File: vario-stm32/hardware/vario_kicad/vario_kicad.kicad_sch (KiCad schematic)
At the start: 2 parts, among them U1 STM32L071CBTx, U2 BME280

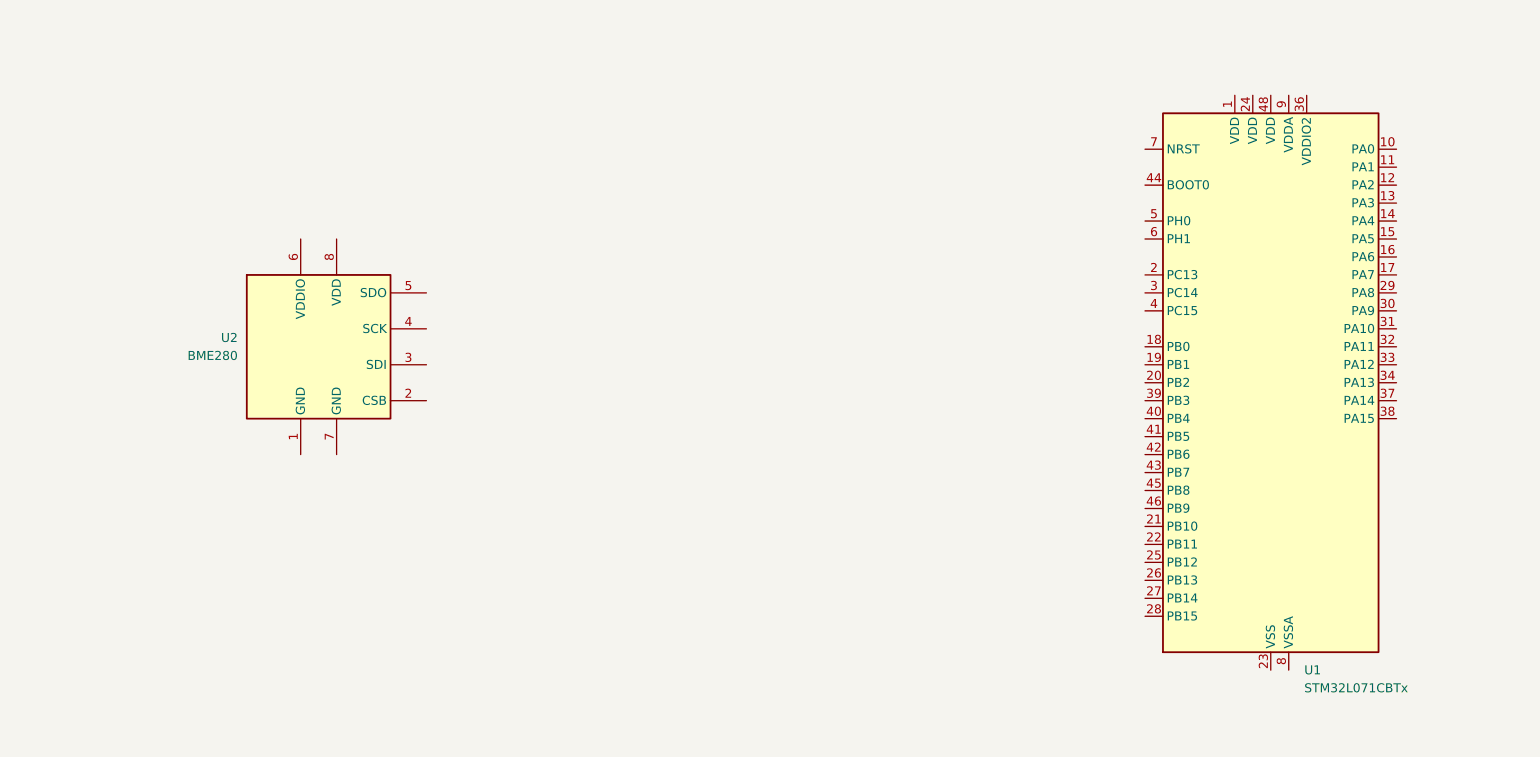
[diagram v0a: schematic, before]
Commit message: update schematic
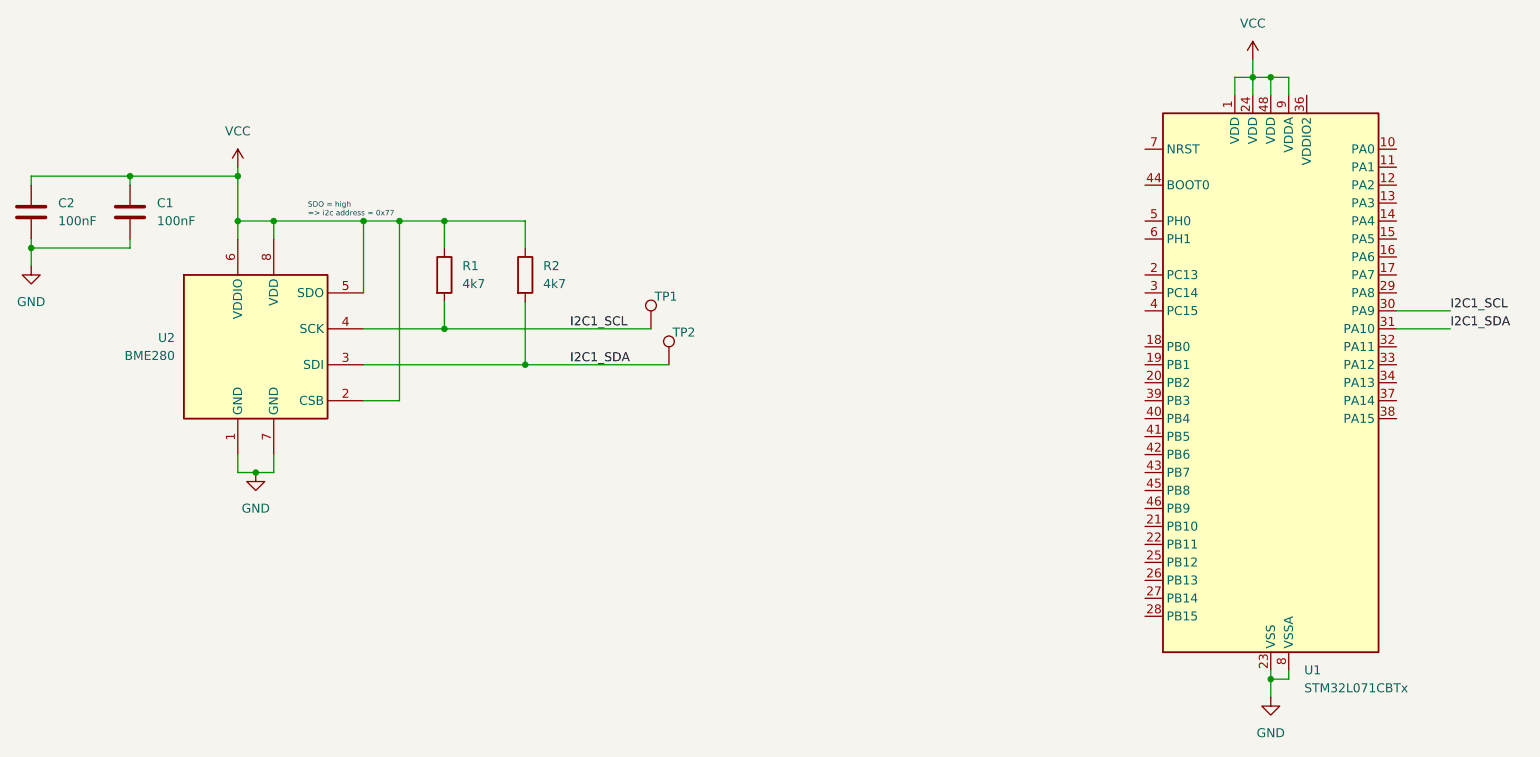
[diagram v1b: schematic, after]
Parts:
- added C1, C2: 100nF, symbol Device:C
- added R1, R2: 4k7, symbol Device:R
- added TP1, TP2: (no value), symbol Connector:TestPoint
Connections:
- net GND: now reaches U2.1 (GND)
- net GND: now also U1.23 (VSS), U1.35 (VSS), U1.47 (VSS), U1.8 (VSSA), U2.7 (GND), C1.2, C2.2
- net VCC: now reaches U2.2 (CSB)
- net VCC: now also U1.1 (VDD), U1.24 (VDD), U1.48 (VDD), U1.9 (VDDA), U2.5 (SDO), U2.6 (VDDIO), U2.8 (VDD), C1.1, C2.1, R1.1, R2.1
- net I2C1_SDA: now reaches U2.3 (SDI)
- net I2C1_SDA: now also U1.31 (PA10), R2.2, TP2.1
- net I2C1_SCL: now reaches U2.4 (SCK)
- net I2C1_SCL: now also U1.30 (PA9), R1.2, TP1.1
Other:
- note added: "SDO = high => i2c address = 0x77"
- moved on the sheet: U2
